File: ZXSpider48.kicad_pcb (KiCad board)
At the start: 2 copper layers, 213.5 x 130.5 mm, 145 parts, among them J1 Barrel_Jack_Switch, J11 EAR/MIC, J12 KB_CONN_05, J14 RESET, J15 ZX_48K_EDGE, J16 DB9_Pins, J17 ON/OFF, J2 JTAG, J3 9V, J4 AUDIO, J5 ROM_SW, J6 M-DIN KMDGX-9S-BS-1, J7 SPK_ON_OFF, J8 KB_CON_08, Q1 BC517, Q10 BC560, Q11 BC560, Q12 BC560, Q13 BC560, Q14 BC560, Q15 BC560, Q2 BC548, Q8 BC560, Q9 BC560, U1 AY-3-8912, U10 27C256, U11 74HCT240, U16 74LS138, U18 74LS00, U2 EPM7128SLC84-10, U3 LM7805_TO220, U4 AY-3-8910, U5 HM62256, U6 74HC04, U7 HM62256, U8 Z80, U9 74LS32, Y2 14.000 Mhz

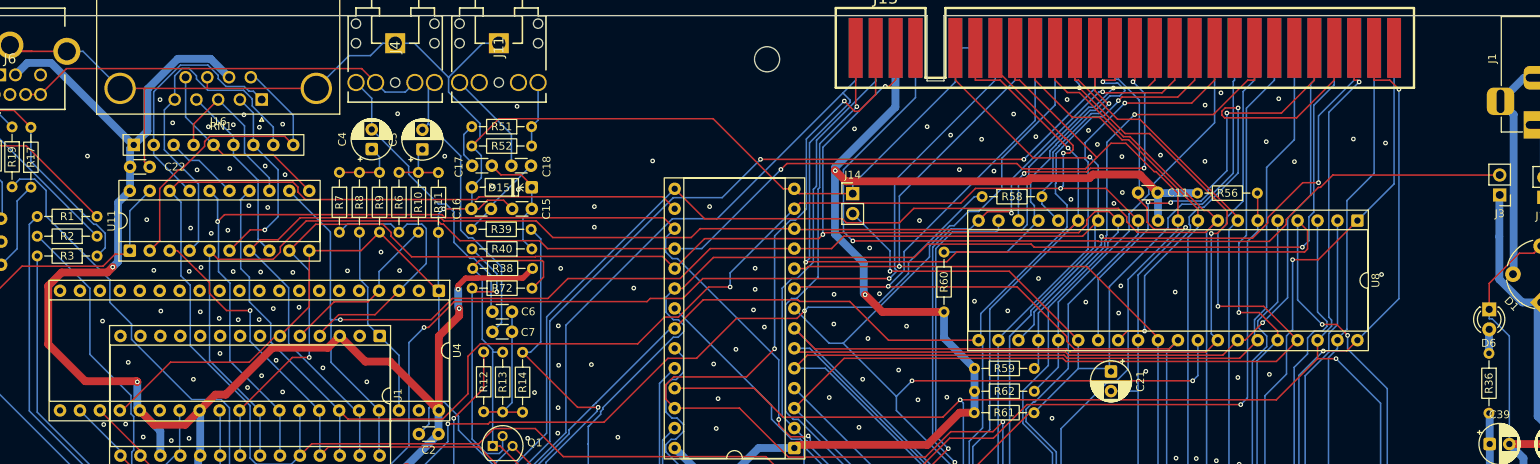
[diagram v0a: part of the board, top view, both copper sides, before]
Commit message: Add files via upload
Added optional +/-12V for IF2 Serial support. Only fit if required.
Added jumper J18 to enable/disable Joystick interface ( fitted to enable, remove to disable).
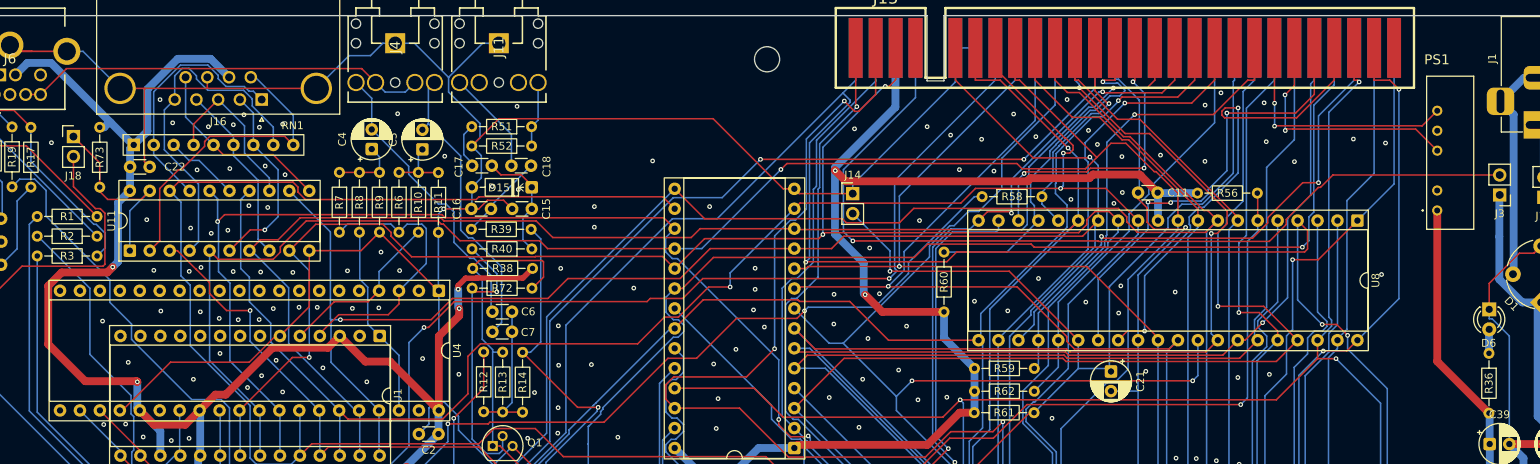
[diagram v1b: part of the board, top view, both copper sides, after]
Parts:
- added J18: JOYSTICK_ON_OFF, Connector_PinHeader_2.54mm:PinHeader_1x02_P2.54mm_Vertical, F.Cu at (42.6, 37.3)
- added PS1: TBA_1-0522E, _MOD:TBA10522E, F.Cu at (216.3, 46.7)
- added R73: 10K, Resistor_THT:R_Axial_DIN0204_L3.6mm_D1.6mm_P7.62mm_Horizontal, F.Cu at (46.0, 43.7)
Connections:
- J15 pad A22: unconnected-(J15-+12-PadA22) -> +12V
- J15 pad A23: unconnected-(J15--12-PadA23) -> -12V
- U11 pad 1: Net-(U11-1OE) -> Net-(J18-Pin_1)
- U11 pad 19: Net-(U11-1OE) -> Net-(J18-Pin_1)
- U9 pad 8: Net-(U11-1OE) -> Net-(J18-Pin_2)
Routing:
- net Net-(J18-Pin_2): track 0.00 -> 123.8 mm, vias 0 -> 1
- net Net-(U11-1OE): track 120.6 -> 0.00 mm, vias 1 -> 0
- net -12V: track 0.00 -> 31.6 mm, vias 0 -> 2
- net +12V: track 0.00 -> 31.5 mm, vias 0 -> 2
- net +5V: track 944.4 -> 974.6 mm
- net Net-(J18-Pin_1): track 0.00 -> 24.9 mm
- net M1: track 56.7 -> 57.8 mm
- net Net-(U1-CH_B): track 34.6 -> 35.6 mm
- net GND: vias 219 -> 224

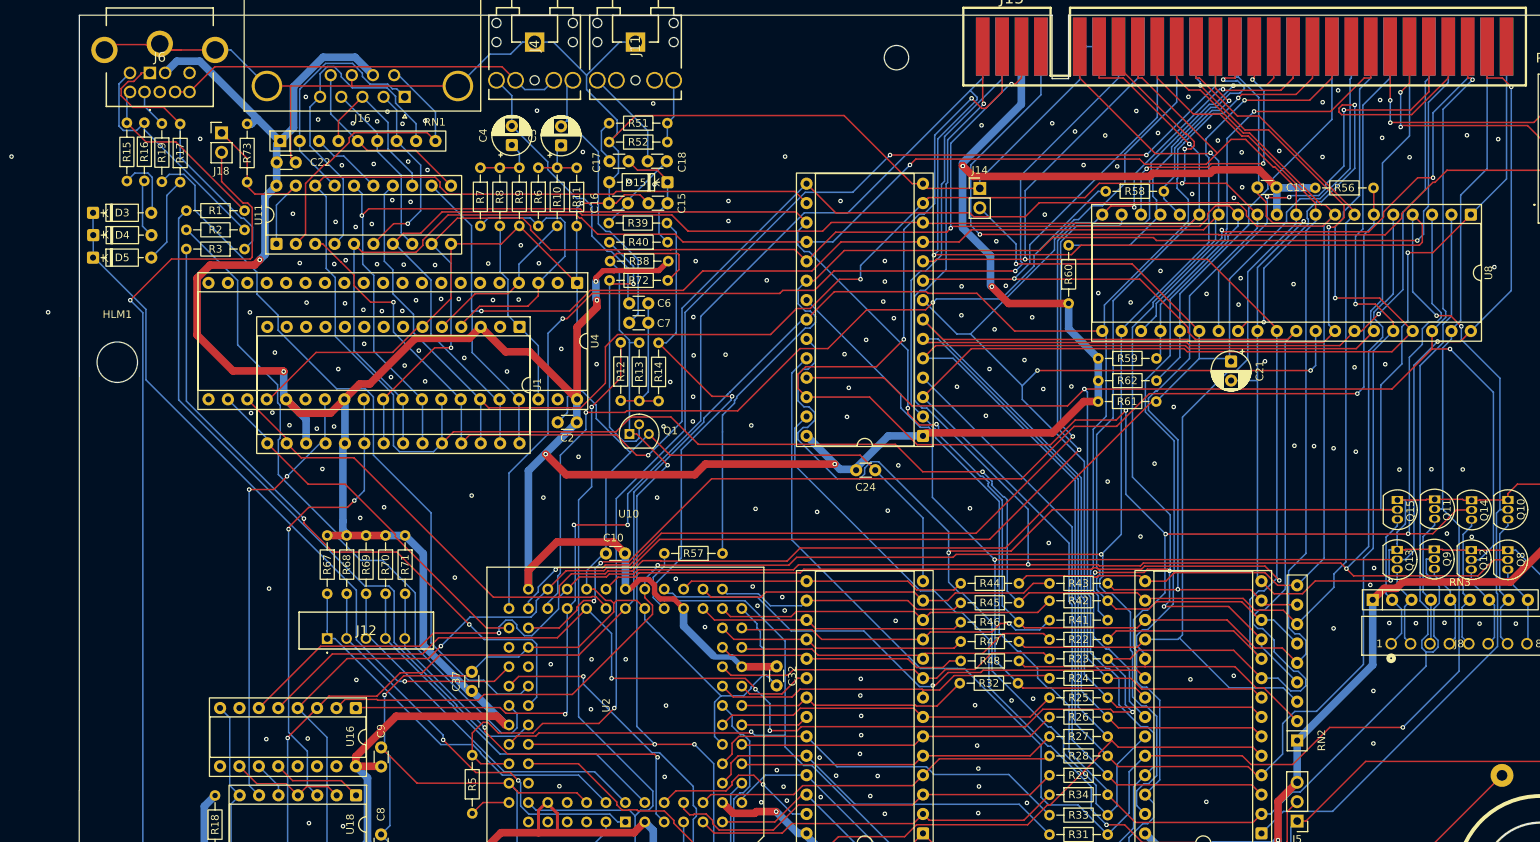
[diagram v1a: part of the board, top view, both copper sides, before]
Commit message: Added header for AY3-8910 IOB (J18) and moved position of U1 and U4
* Routed AY3-8910 IOB Bits0-7 to header   J18 Pins  1(Bit0)- 8(Bit7)
* AY3-8910 IOA Bits 0-7 can be picked from U1 pins  7(Bit7)-14(Bit0)
* AY3-8912 IOA Bits 1-7 can be picked from U4 Pins 14(Bit7)-20(Bit1)
* AY3-8912 IOA Bit0 can be picked from J20
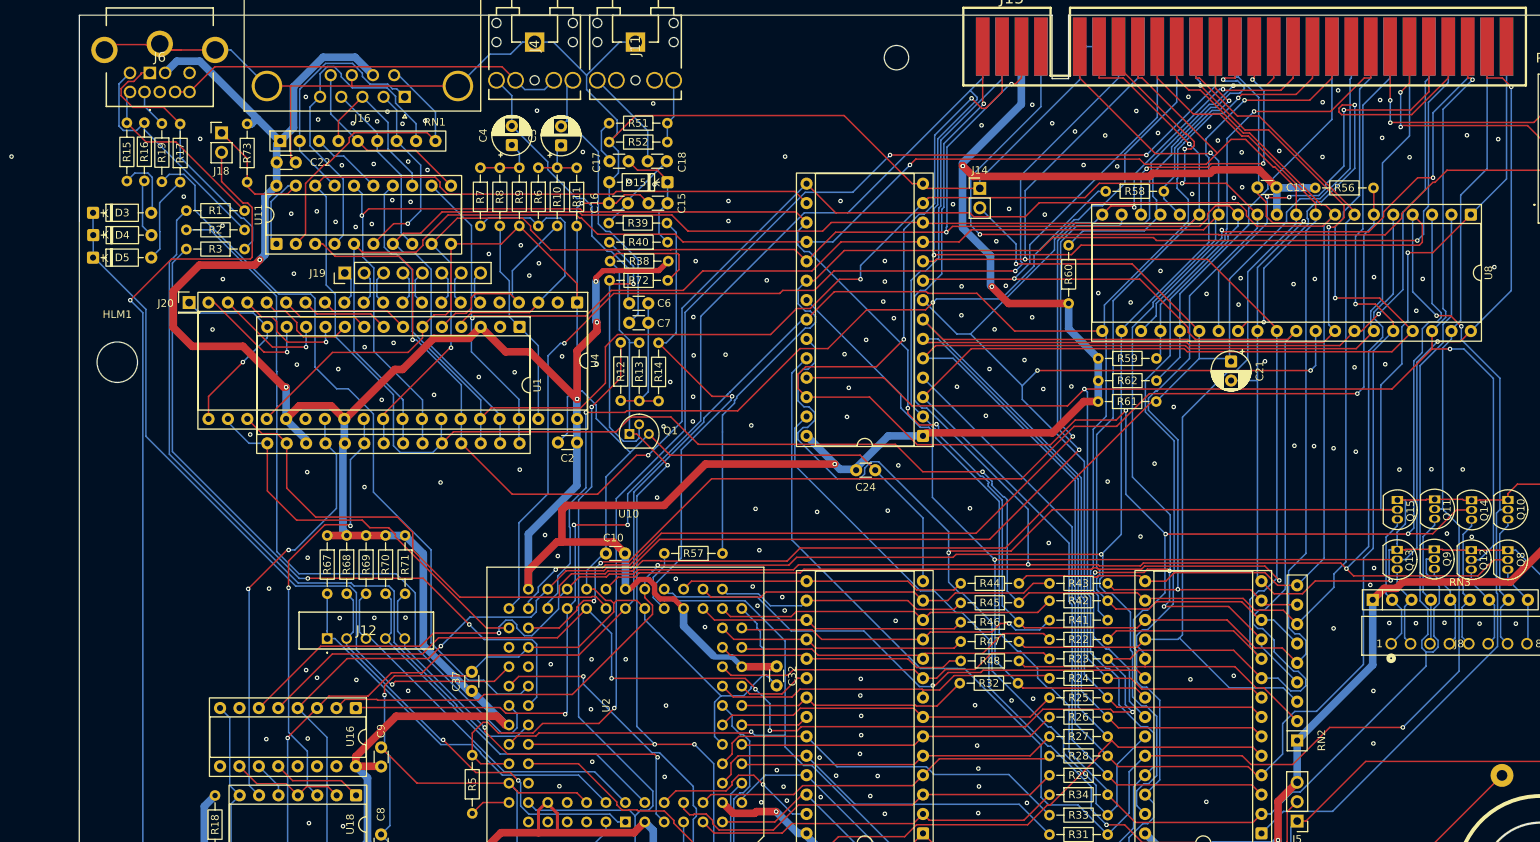
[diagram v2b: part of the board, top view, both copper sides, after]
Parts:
- added J19: AY3_IOB, Connector_PinHeader_2.54mm:PinHeader_1x08_P2.54mm_Vertical, F.Cu at (58.7, 55.6)
- added J20: Conn_01x01, Connector_PinHeader_2.54mm:PinHeader_1x01_P2.54mm_Vertical, F.Cu at (38.4, 59.5)
- moved C2 2.65 mm to (89.2, 77.8)
- moved U4 2.57 mm to (89.2, 59.5)
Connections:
- U1 pad 10: unconnected-(U1-IOA4-Pad10) -> IOA4
- U1 pad 11: unconnected-(U1-IOA3-Pad11) -> IOA3
- U1 pad 12: unconnected-(U1-IOA2-Pad12) -> IOA2
- U1 pad 13: unconnected-(U1-IOA1-Pad13) -> IOA1
- U1 pad 14: unconnected-(U1-IOA0-Pad14) -> IOA0
- U1 pad 7: unconnected-(U1-IOA7-Pad7) -> IOA7
- U1 pad 8: unconnected-(U1-IOA6-Pad8) -> IOA6
- U1 pad 9: unconnected-(U1-IOA5-Pad9) -> IOA5
- U4 pad 10: unconnected-(U4-IOB3-Pad10) -> IOB3
- U4 pad 11: unconnected-(U4-IOB2-Pad11) -> IOB2
- U4 pad 12: unconnected-(U4-IOB1-Pad12) -> IOB1
- U4 pad 13: unconnected-(U4-IOB0-Pad13) -> IOB0
- U4 pad 14: unconnected-(U4-IOA7-Pad14) -> IOA7
- U4 pad 15: unconnected-(U4-IOA6-Pad15) -> IOA6
- U4 pad 16: unconnected-(U4-IOA5-Pad16) -> IOA5
- U4 pad 17: unconnected-(U4-IOA4-Pad17) -> IOA4
- U4 pad 18: unconnected-(U4-IOA3-Pad18) -> IOA3
- U4 pad 19: unconnected-(U4-IOA2-Pad19) -> IOA2
- U4 pad 20: unconnected-(U4-IOA1-Pad20) -> IOA1
- U4 pad 21: unconnected-(U4-IOA0-Pad21) -> IOA0
- U4 pad 6: unconnected-(U4-IOB7-Pad6) -> IOB7
- U4 pad 7: unconnected-(U4-IOB6-Pad7) -> IOB6
- U4 pad 8: unconnected-(U4-IOB5-Pad8) -> IOB5
- U4 pad 9: unconnected-(U4-IOB4-Pad9) -> IOB4
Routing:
- net IOA0: track 0.00 -> 26.8 mm, vias 0 -> 1
- net IOA1: track 0.00 -> 16.3 mm, vias 0 -> 1
- net IOA2: track 0.00 -> 15.3 mm, vias 0 -> 1
- net IOA3: track 0.00 -> 15.2 mm, vias 0 -> 1
- net IOA4: track 0.00 -> 13.2 mm
- net IOA7: track 0.00 -> 11.6 mm
- net IOA6: track 0.00 -> 11.6 mm
- net IOA5: track 0.00 -> 11.6 mm
- net GND: track 1011.3 -> 1020.0 mm
- net GREEN: track 90.6 -> 97.8 mm
- net D3: track 301.8 -> 308.6 mm
- net BLUE: track 87.8 -> 93.9 mm
- net RED: track 93.8 -> 99.7 mm
- net BRIGHT: track 93.3 -> 98.6 mm
- net +5V: track 974.6 -> 969.4 mm
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
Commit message: Add files via upload
Changed ROM select to 2 pin rather than 3 pin header
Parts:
- added R74: 10K, Resistor_THT:R_Axial_DIN0204_L3.6mm_D1.6mm_P7.62mm_Horizontal, F.Cu at (186.9, 117.1)
- J20: value Conn_01x01 -> AY3_IOA; footprint Connector_PinHeader_2.54mm:PinHeader_1x01_P2.54mm_Vertical -> Connector_PinHeader_2.54mm:PinHeader_1x08_P2.54mm_Vertical
- J5: footprint Connector_PinHeader_2.54mm:PinHeader_1x03_P2.54mm_Vertical -> Connector_PinHeader_2.54mm:PinHeader_1x02_P2.54mm_Vertical
- moved J20 3.89 mm to (38.0, 55.6), turned to 90 degrees
- moved D5 1.12 mm to (25.8, 52.5)
- moved D4 0.69 mm to (25.8, 50.0)
- moved D3 0.28 mm to (25.8, 47.5)
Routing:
- net D6: track 290.3 -> 296.7 mm
- net +5V: track 969.4 -> 975.2 mm, vias 11 -> 12
- net IOA4: track 13.2 -> 17.3 mm
- net IOA6: track 11.6 -> 15.6 mm
- net IOA3: track 15.2 -> 19.2 mm
- net IOA1: track 16.3 -> 20.3 mm
- net IOA0: track 26.8 -> 30.8 mm
- net IOA5: track 11.6 -> 15.6 mm
- net IOA7: track 11.6 -> 15.6 mm
- net IOA2: track 15.3 -> 19.3 mm
- net Net-(J5-Pin_2): track 104.4 -> 108.0 mm
- net Net-(J18-Pin_2): track 123.8 -> 122.2 mm
- net GREEN: track 97.8 -> 99.1 mm
- net Net-(D5-A): track 11.5 -> 10.4 mm
- net A5: track 290.4 -> 291.2 mm
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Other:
- board text added: "+/-12V"
- board text added: "27C256"
- board text added: "74HC04"
- board text added: "74HCT240"
- board text added: "74LS00"
- board text added: "74LS138"
- board text added: "74LS32"
- board text added: "AY-3-89XX"
- board text added: "EPM7128SLC84"
- board text added: "HM62256"
- board text added: "IOA0-7"
- board text added: "IOB0-7"
- board text added: "Z80 CPU"
